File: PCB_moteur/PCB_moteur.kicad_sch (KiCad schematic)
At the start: 0 parts

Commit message: Début schéma moteurs
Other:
- added sheet Interfaces (Interfaces_moteur.kicad_sch)
- added sheet STM32 (STM32_moteur.kicad_sch)
- added sheet Supply (Supply_moteur.kicad_sch)
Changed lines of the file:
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@@
 	(generator_version "9.0")
 	(paper "A4")
+	(sheet
+		(at 99.06 16.51)
+		(size 77.47 67.31)
+		(exclude_from_sim no)
+		(in_bom yes)
+		(on_board yes)
+		(dnp no)
+		(fields_autoplaced yes)
+		(stroke
+			(width 0.1524)
+			(type solid)
+		)
+		(fill
+			(color 0 0 0 0.0000)
+		)
+		(property "Sheetname" "STM32"
+			(at 99.06 15.7984 0)
+			(effects
+				(font
+					(size 1.27 1.27)
+				)
+				(justify left bottom)
+			)
+		)
+		(property "Sheetfile" "STM32_moteur.kicad_sch"
+			(at 99.06 84.4046 0)
+			(effects
+				(font
+					(size 1.27 1.27)
+				)
+				(justify left top)
+			)
+		)
+		(instances
+			(project "PCB_moteur"
+				(path "/b0d87684-7b1c-41d8-8358-755aa327573e"
+					(page "3")
+				)
+			)
+		)
+	)
+	(sheet
+		(at 16.51 16.51)
+		(size 73.66 67.31)
+		(exclude_from_sim no)
+		(in_bom yes)
+		(on_board yes)
+		(dnp no)
+		(fields_autoplaced yes)
+		(stroke
+			(width 0.1524)
+			(type solid)
+		)
+		(fill
+			(color 0 0 0 0.0000)
+		)
+		(property "Sheetname" "Supply"
+			(at 16.51 15.7984 0)
+			(effects
+				(font
+					(size 1.27 1.27)
+				)
+				(justify left bottom)
+			)
+		)
+		(property "Sheetfile" "Supply_moteur.kicad_sch"
+			(at 16.51 84.4046 0)
+			(effects
+				(font
+					(size 1.27 1.27)
+				)
+				(justify left top)
+			)
+		)
+		(instances
+			(project "PCB_moteur"
+				(path "/b0d87684-7b1c-41d8-8358-755aa327573e"
+					(page "2")
+				)
+			)
+		)
+	)
+	(sheet
+		(at 186.69 17.78)
+		(size 77.47 66.04)
+		(exclude_from_sim no)
+		(in_bom yes)
+		(on_board yes)
+		(dnp no)
+		(fields_autoplaced yes)
+		(stroke
+			(width 0.1524)
+			(type solid)
+		)
+		(fill
+			(color 0 0 0 0.0000)
+		)
+		(property "Sheetname" "Interfaces"
+			(at 186.69 17.0684 0)
+			(effects
+				(font
+					(size 1.27 1.27)
+				)
+				(justify left bottom)
+			)
+		)
+		(property "Sheetfile" "Interfaces_moteur.kicad_sch"
+			(at 186.69 84.4046 0)
+			(effects
+				(font
+					(size 1.27 1.27)
+				)
+				(justify left top)
+			)
+		)
+		(instances
+			(project "PCB_moteur"
+				(path "/b0d87684-7b1c-41d8-8358-755aa327573e"
+					(page "4")
+				)
+			)
+		)
+	)
 	(sheet_instances
 		(path "/"

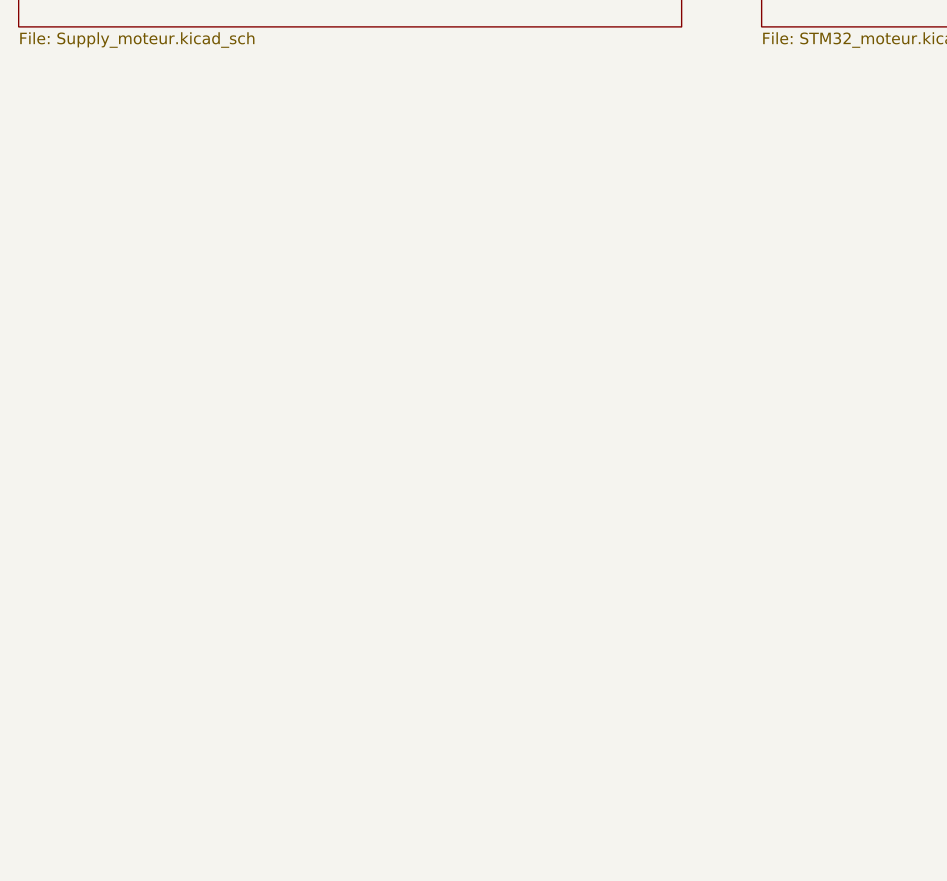
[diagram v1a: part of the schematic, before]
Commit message: Manque supply, pyro et finition (découplage etc)
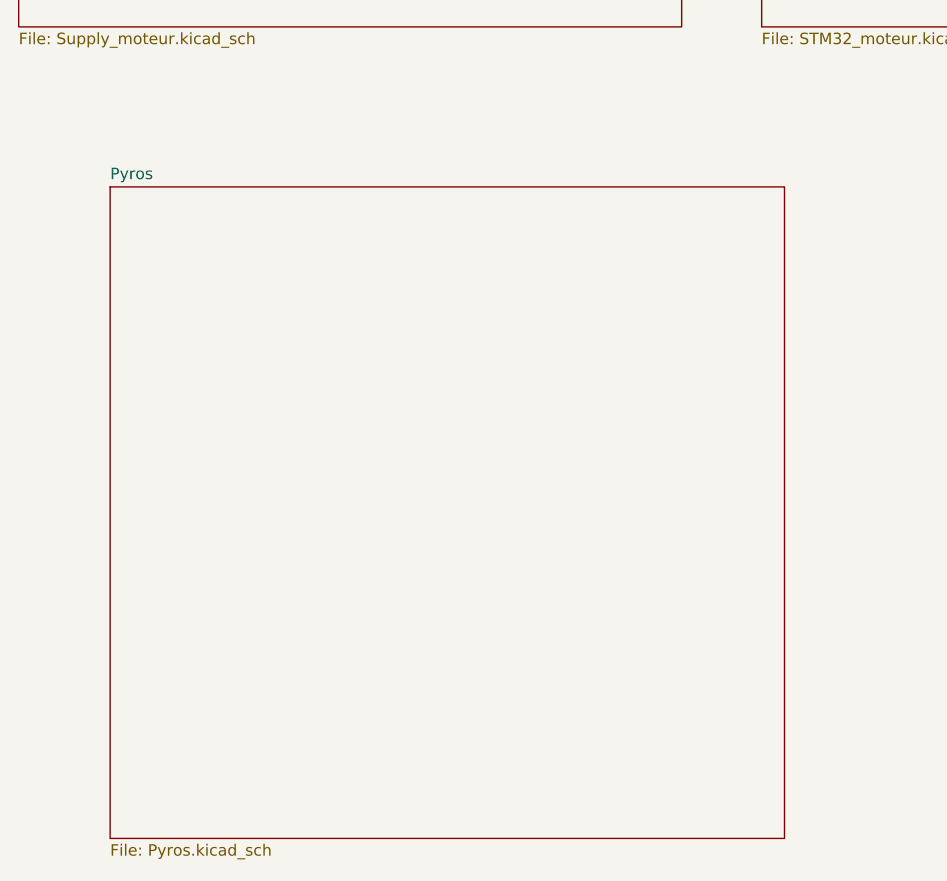
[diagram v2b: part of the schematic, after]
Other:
- added sheet Pyros (Pyros.kicad_sch)
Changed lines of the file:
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@@
 	(paper "A4")
+	(sheet
+		(at 26.67 101.6)
+		(size 74.93 72.39)
+		(exclude_from_sim no)
+		(in_bom yes)
+		(on_board yes)
+		(dnp no)
+		(fields_autoplaced yes)
+		(stroke
+			(width 0.1524)
+			(type solid)
+		)
+		(fill
+			(color 0 0 0 0.0000)
+		)
+		(property "Sheetname" "Pyros"
+			(at 26.67 100.8884 0)
+			(effects
+				(font
+					(size 1.27 1.27)
+				)
+				(justify left bottom)
+			)
+		)
+		(property "Sheetfile" "Pyros.kicad_sch"
+			(at 26.67 174.5746 0)
+			(effects
+				(font
+					(size 1.27 1.27)
+				)
+				(justify left top)
+			)
+		)
+		(instances
+			(project "PCB_moteur"
+				(path "/b0d87684-7b1c-41d8-8358-755aa327573e"
+					(page "5")
+				)
+			)
+		)
+	)
 	(sheet
 		(at 99.06 16.51)

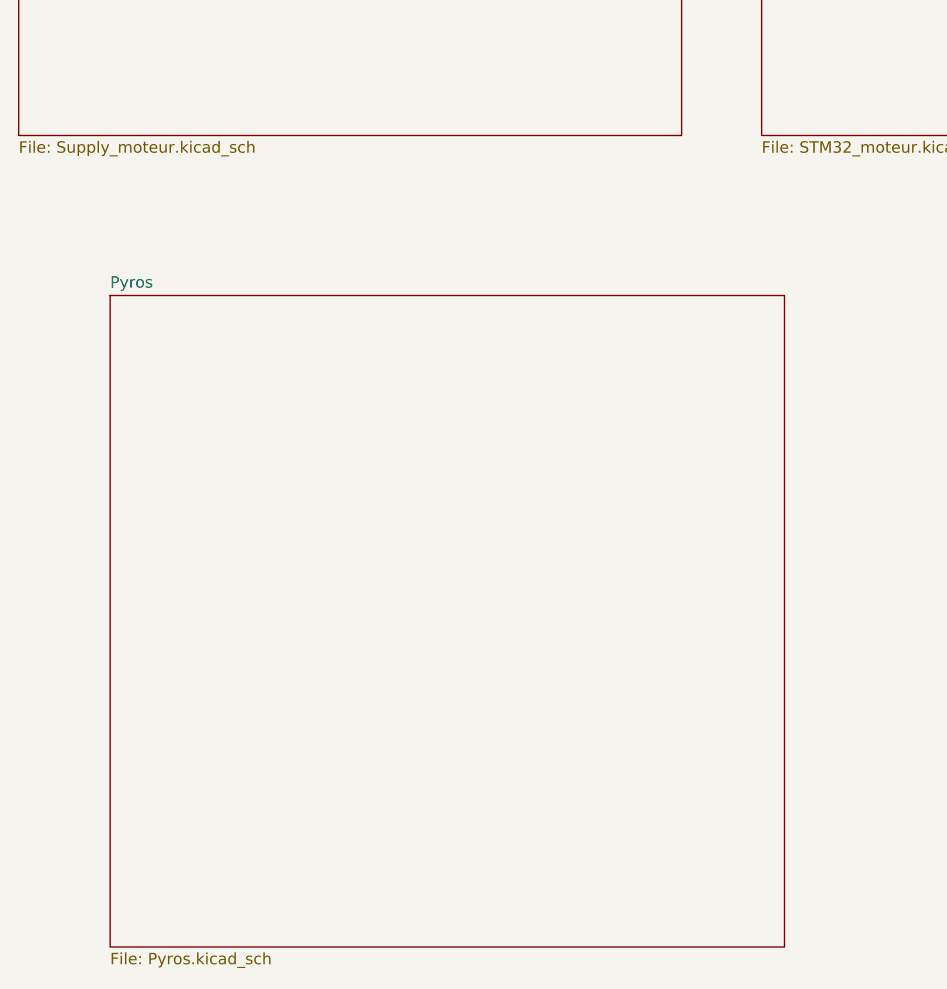
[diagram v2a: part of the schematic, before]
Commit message: wip: remove unnecessary components
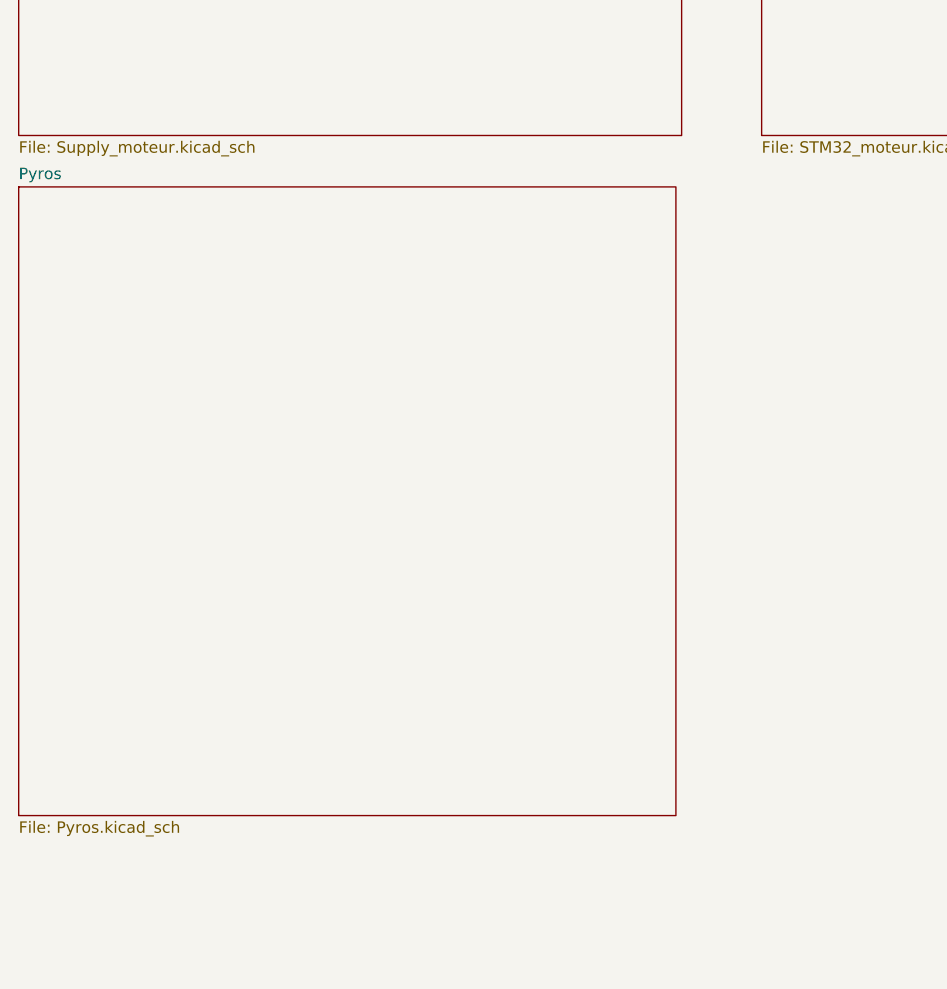
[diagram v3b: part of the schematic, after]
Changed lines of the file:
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@@
 	(paper "A4")
 	(sheet
-		(at 26.67 101.6)
-		(size 74.93 72.39)
+		(at 16.51 89.535)
+		(size 73.025 69.85)
 		(exclude_from_sim no)
 		(in_bom yes)
@@
 		)
 		(property "Sheetname" "Pyros"
-			(at 26.67 100.8884 0)
+			(at 16.51 88.8234 0)
 			(effects
 				(font
@@
 		)
 		(property "Sheetfile" "Pyros.kicad_sch"
-			(at 26.67 174.5746 0)
+			(at 16.51 159.9696 0)
 			(effects
 				(font

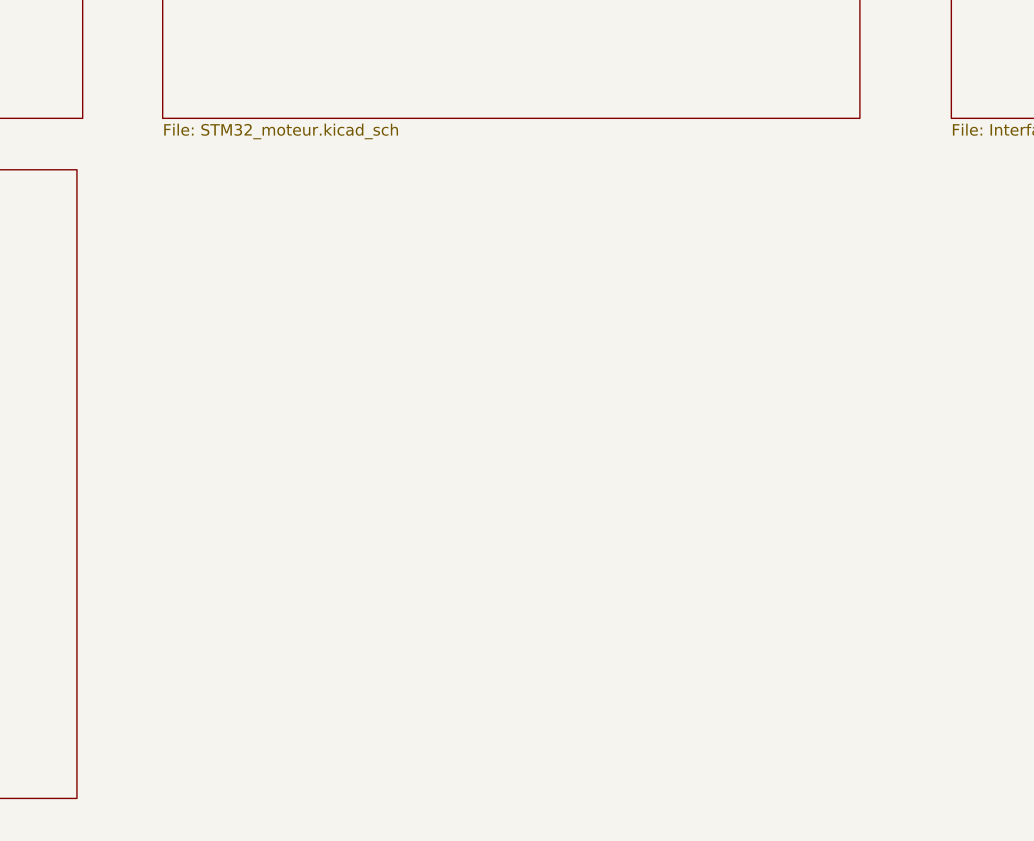
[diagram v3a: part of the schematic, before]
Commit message: Added LDO, INA125, sensors
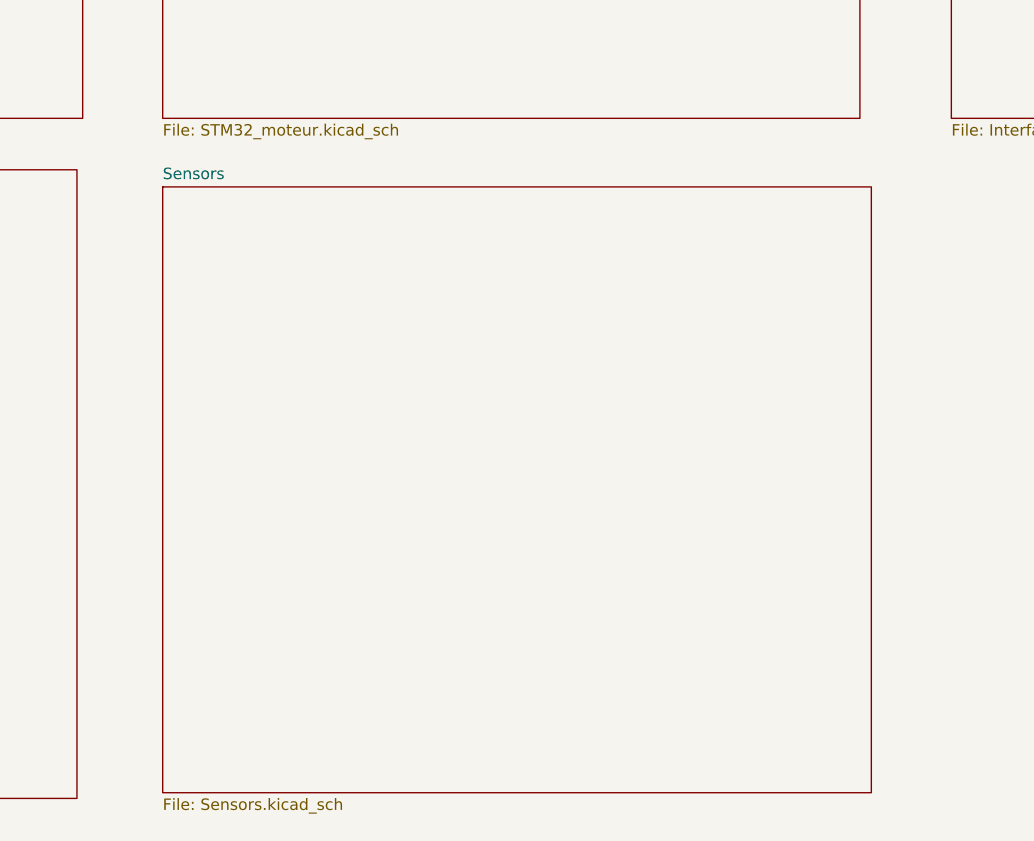
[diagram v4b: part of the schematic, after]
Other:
- added sheet Sensors (Sensors.kicad_sch)
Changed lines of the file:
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@@
+		)
+	)
+	(sheet
+		(at 99.06 91.44)
+		(size 78.74 67.31)
+		(exclude_from_sim no)
+		(in_bom yes)
+		(on_board yes)
+		(dnp no)
+		(fields_autoplaced yes)
+		(stroke
+			(width 0.1524)
+			(type solid)
+		)
+		(fill
+			(color 0 0 0 0.0000)
+		)
+		(property "Sheetname" "Sensors"
+			(at 99.06 90.7284 0)
+			(effects
+				(font
+					(size 1.27 1.27)
+				)
+				(justify left bottom)
+			)
+		)
+		(property "Sheetfile" "Sensors.kicad_sch"
+			(at 99.06 159.3346 0)
+			(effects
+				(font
+					(size 1.27 1.27)
+				)
+				(justify left top)
+			)
+		)
+		(instances
+			(project "PCB_moteur"
+				(path "/b0d87684-7b1c-41d8-8358-755aa327573e"
+					(page "6")
+				)
+			)
 		)
 	)
